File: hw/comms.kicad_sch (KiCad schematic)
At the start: 13 parts, among them J7 CAN IN, J8 CAN OUT, J9 USB-C, SW1 TERM, U6 TCAN3413, U7 USBLC6-2SC6

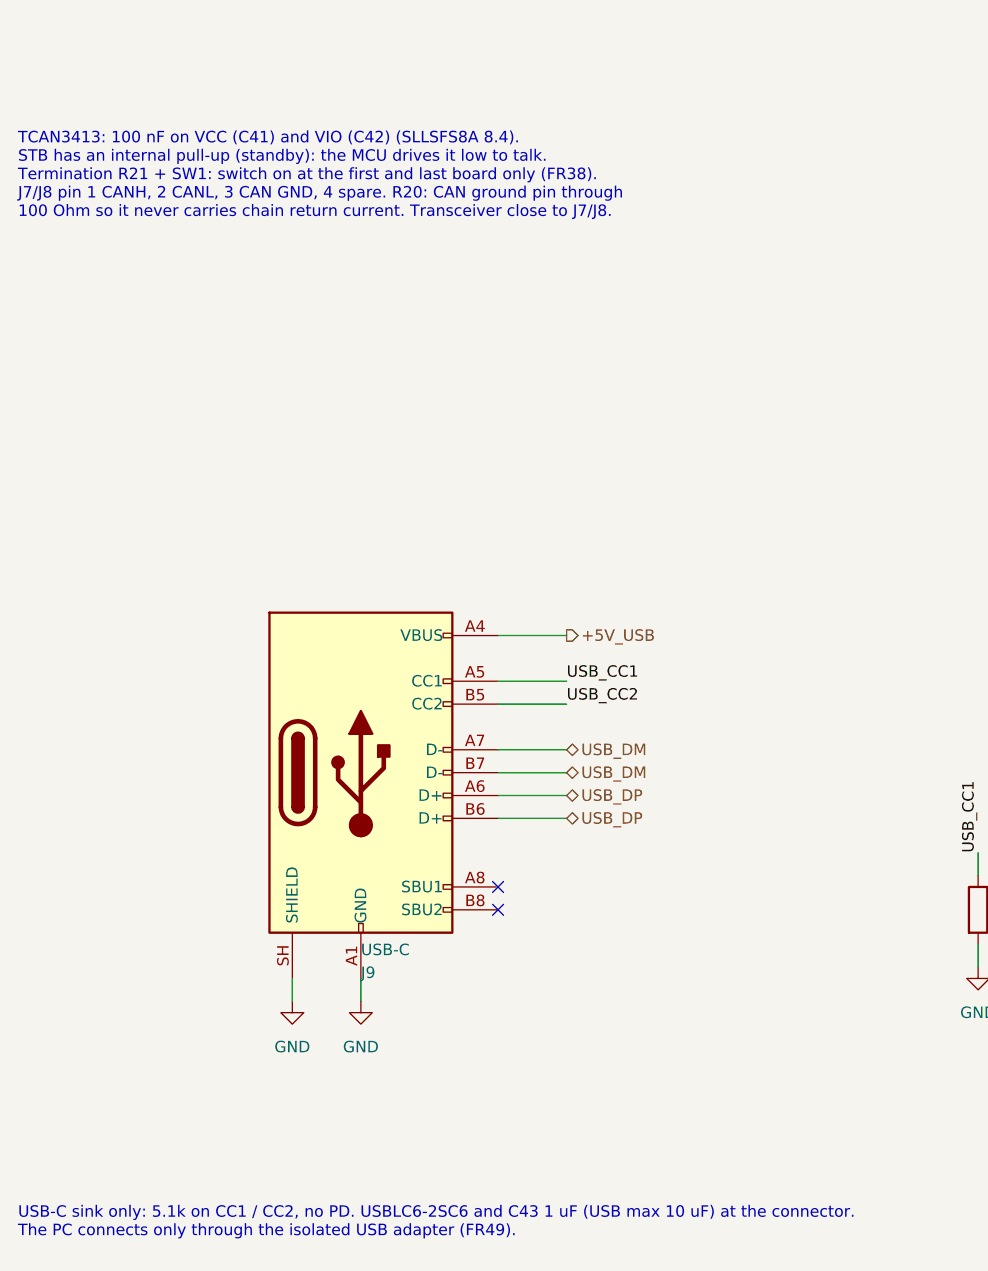
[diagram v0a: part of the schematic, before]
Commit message: Remove requirement IDs from schematic notes
Notes now state the reason in plain words so the schematic reads
without the requirements document.

Co-Authored-By: Claude Opus 5.5 <noreply@anthropic.com>
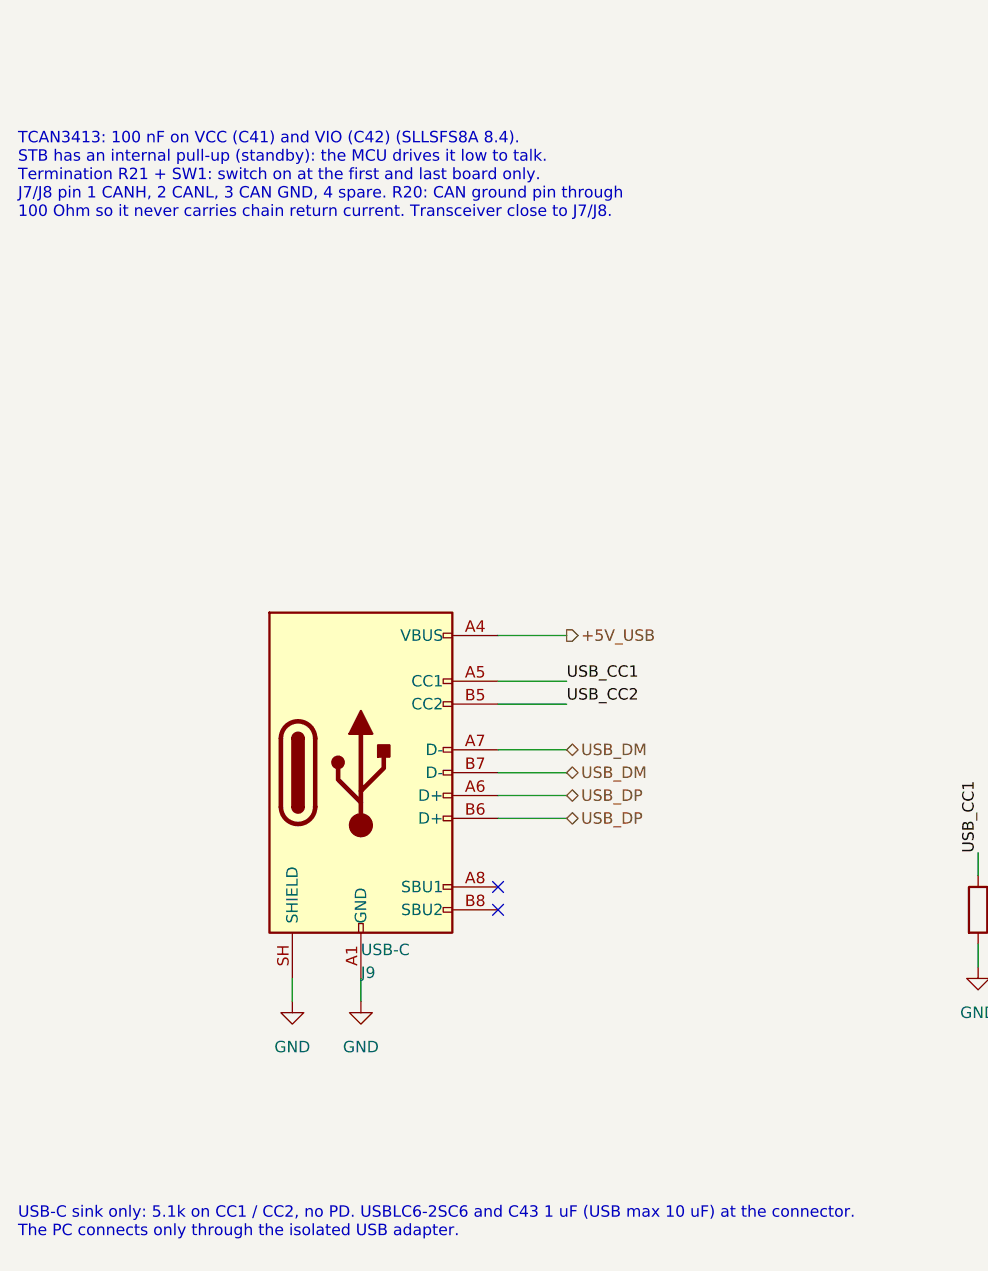
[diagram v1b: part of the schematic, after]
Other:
- note added: "TCAN3413: 100 nF on VCC (C41) and VIO (C42) (SLLSFS8A 8.4). STB has an internal pull-up (standby): the MCU drives it low to talk. Termination R21 + SW1: switch on at the first and last board only. J7/J8 pin 1 CANH, 2 CANL, 3 CAN GND, 4 spare. R20: CAN ground pin through 100 Ohm so it never carries chain return current. Transceiver close to J7/J8."
- note added: "USB-C sink only: 5.1k on CC1 / CC2, no PD. USBLC6-2SC6 and C43 1 uF (USB max 10 uF) at the connector. The PC connects only through the isolated USB adapter."
- note removed: "TCAN3413: 100 nF on VCC (C41) and VIO (C42) (SLLSFS8A 8.4). STB has an internal pull-up (standby): the MCU drives it low to talk. Termination R21 + SW1: switch on at the first and last board only (FR38). J7/J8 pin 1 CANH, 2 CANL, 3 CAN GND, 4 spare. R20: CAN ground pin through 100 Ohm so it never carries chain return current. Transceiver close to J7/J8."
- note removed: "USB-C sink only: 5.1k on CC1 / CC2, no PD. USBLC6-2SC6 and C43 1 uF (USB max 10 uF) at the connector. The PC connects only through the isolated USB adapter (FR49)."
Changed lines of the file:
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@@
 		(at 78.74 228.6)
 	)
-	(text "TCAN3413: 100 nF on VCC (C41) and VIO (C42) (SLLSFS8A 8.4).\nSTB has an internal pull-up (standby): the MCU drives it low to talk.\nTermination R21 + SW1: switch on at the first and last board only (FR38).\nJ7/J8 pin 1 CANH, 2 CANL, 3 CAN GND, 4 spare. R20: CAN ground pin through\n100 Ohm so it never carries chain return current. Transceiver close to J7/J8."
+	(text "TCAN3413: 100 nF on VCC (C41) and VIO (C42) (SLLSFS8A 8.4).\nSTB has an internal pull-up (standby): the MCU drives it low to talk.\nTermination R21 + SW1: switch on at the first and last board only.\nJ7/J8 pin 1 CANH, 2 CANL, 3 CAN GND, 4 spare. R20: CAN ground pin through\n100 Ohm so it never carries chain return current. Transceiver close to J7/J8."
 		(exclude_from_sim no)
 		(at 25.4 142.24 0.0000)
@@
 		)
 	)
-	(text "USB-C sink only: 5.1k on CC1 / CC2, no PD. USBLC6-2SC6 and C43 1 uF (USB max 10 uF) at the connector.\nThe PC connects only through the isolated USB adapter (FR49)."
+	(text "USB-C sink only: 5.1k on CC1 / CC2, no PD. USBLC6-2SC6 and C43 1 uF (USB max 10 uF) at the connector.\nThe PC connects only through the isolated USB adapter."
 		(exclude_from_sim no)
 		(at 25.4 261.62 0.0000)
